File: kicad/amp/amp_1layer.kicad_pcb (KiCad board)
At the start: 2 copper layers, 145 x 120.3 mm, 126 parts, among them J1 DC 12V IN, J2 IN L-G-R, J3 SPK L, J4 SPK R, Q1001 BC547, Q1002 BC547, Q1003 BC557, Q1004 BD139, Q1005 BD140, Q1006 BC547, Q2001 BC547, Q2002 BC547, Q2003 BC557, Q2004 BD139, Q2005 BD140, Q2006 BC547

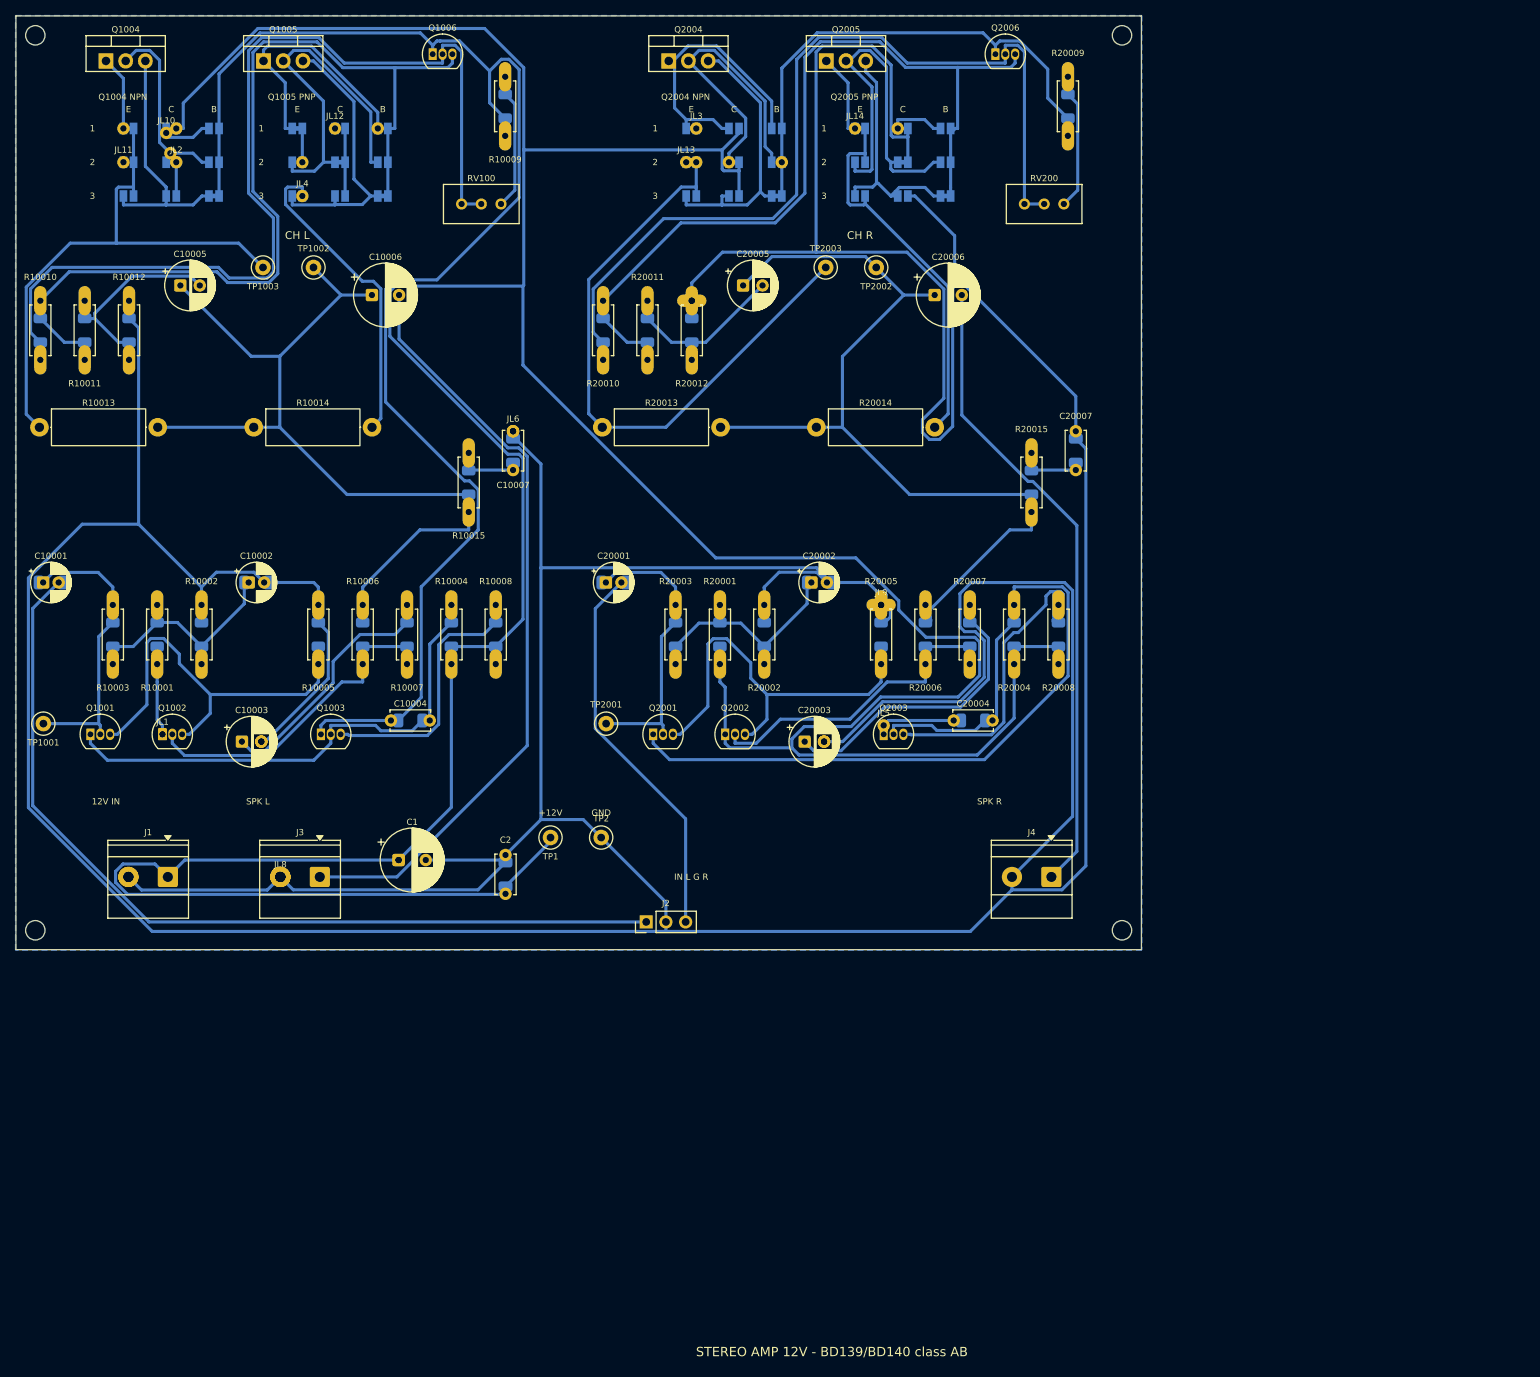
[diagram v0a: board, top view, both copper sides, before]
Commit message: Rotate screw terminals to face the board edge, add 3D views, schematics and layouts to the README, CircuitJS links in the review
Amp board is 100 x 85 mm after the hybrid-footprint courtyards grew; input header moved to open space
on the bottom edge so freerouting completes. Panel 134 x 137 mm, DRC clean.
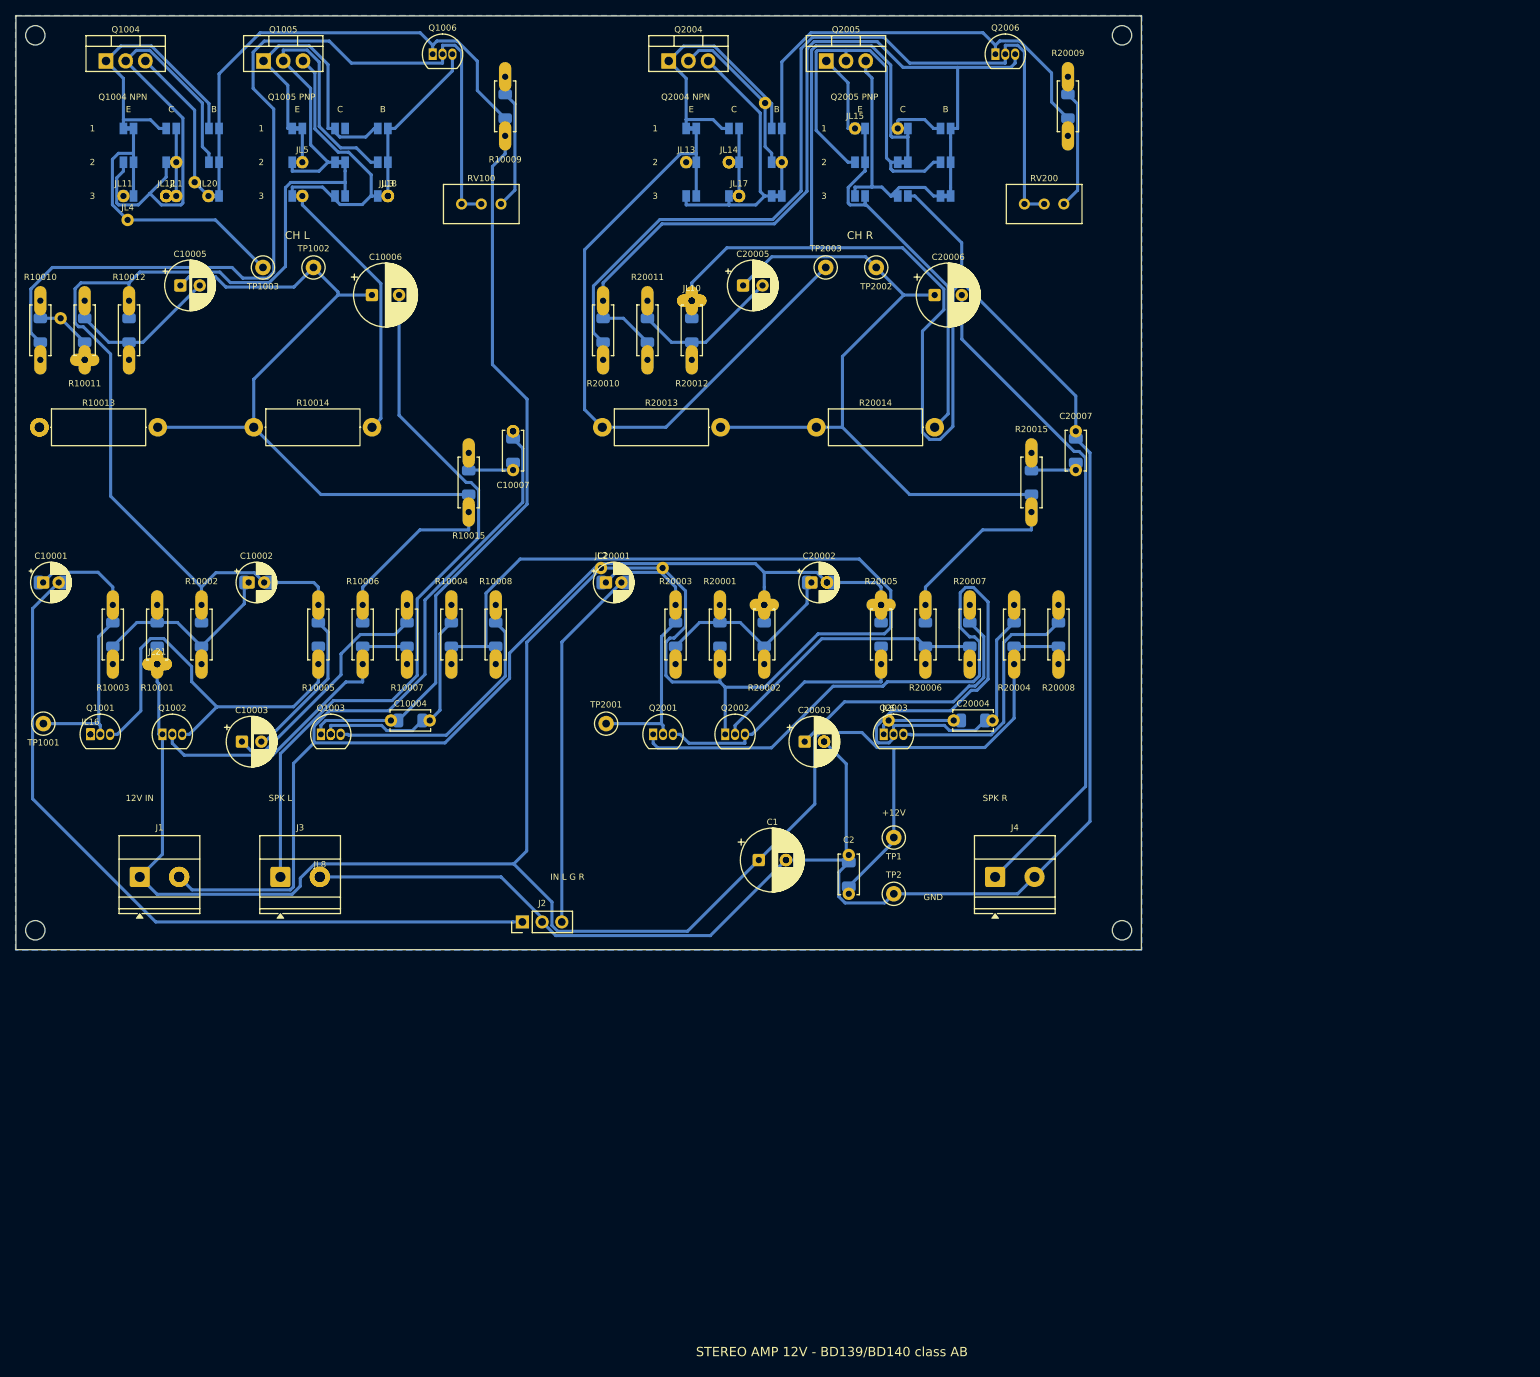
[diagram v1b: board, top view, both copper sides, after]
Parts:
- added JL15: wire link, Custom:WireLink, F.Cu at (158.1, 64.5)
- added JL16: wire link, Custom:WireLink, F.Cu at (59.6, 142.6)
- added JL17: wire link, Custom:WireLink, F.Cu at (143.2, 73.2)
- added JL18: wire link, Custom:WireLink, F.Cu at (97.9, 73.2)
- added JL19: wire link, Custom:WireLink, F.Cu at (149.2, 158.8)
- added JL20: wire link, Custom:WireLink, F.Cu at (74.8, 73.2)
- added JL21: wire link, Custom:WireLink, F.Cu at (68.2, 133.5)
- moved JL5 104.3 mm to (86.9, 68.8)
- moved JL2 75.7 mm to (125.4, 121.1)
- moved JL7 72.5 mm to (154.1, 143.5)
- moved JL10 71.1 mm to (137.1, 86.7)
- moved JL1 69.4 mm to (70.7, 73.2)
- moved JL6 61.1 mm to (162.4, 140.8)
- moved C1 46.4 mm to (145.7, 158.8)
- moved C2 44.2 mm to (157.3, 163.1)
- moved TP1 44.2 mm to (163.1, 155.8)
- moved JL3 40.7 mm to (97.9, 73.2)
- moved TP2 38.4 mm to (163.1, 163.1)
- moved JL12 23.4 mm to (69.4, 73.2)
- moved JL4 22.7 mm to (64.4, 76.3)
- moved JL14 16.8 mm to (141.9, 68.8)
- moved J2 15.9 mm to (115.2, 166.7)
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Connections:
- JL10 pad 1: Net-(JP10001-A) -> GND
- JL10 pad 2: Net-(JP10001-A) -> GND
- JL11 pad 1: Net-(JP10004-A) -> Net-(JP10007-A)
- JL11 pad 2: Net-(JP10004-A) -> Net-(JP10007-A)
- JL12 pad 1: Net-(JP10014-A) -> Net-(JP10007-A)
- JL12 pad 2: Net-(JP10014-A) -> Net-(JP10007-A)
- JL14 pad 1: Net-(JP20014-A) -> Net-(JP20004-A)
- JL14 pad 2: Net-(JP20014-A) -> Net-(JP20004-A)
- JL3 pad 1: /E4_R -> /B5_L
- JL3 pad 2: /E4_R -> /B5_L
- JL4 pad 1: /E5_L -> /E4_L
- JL4 pad 2: /E5_L -> /E4_L
- JL5 pad 1: /VAS_R -> /E5_L
- JL5 pad 2: /VAS_R -> /E5_L
- JL6 pad 1: GND -> /VAS_R
- JL6 pad 2: GND -> /VAS_R
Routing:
- net GND: track 828.3 -> 698.4 mm
- net +12V: track 535.2 -> 414.6 mm
- net /B5_L: track 121.0 -> 33.8 mm
- net Net-(JP10004-A): track 24.8 -> 63.0 mm
- net Net-(Q1001-C): track 65.9 -> 30.8 mm
- net /E4_L: track 70.9 -> 40.3 mm
- net /VAS_L: track 185.7 -> 161.5 mm
- net Net-(JP10001-A): track 16.8 -> 36.0 mm
- net Net-(JP20004-A): track 38.4 -> 21.2 mm
- net Net-(Q2001-E): track 52.9 -> 35.8 mm
- net /IN_L: track 115.9 -> 99.5 mm
- net Net-(Q2001-C): track 111.0 -> 126.5 mm
- net Net-(JP10007-A): track 32.3 -> 20.8 mm
- net /E4_R: track 80.2 -> 89.3 mm
- net Net-(Q2003-E): track 43.2 -> 34.3 mm
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
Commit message: Square 144 x 144 mm panel with rails; amp widened to 134 x 71 mm so PSU plus volume board match its width; readable silkscreen
References sit inside resistor, diode and ceramic outlines along the body axis, larger text; electrolytic,
transistor and test-point labels stay beside the part. Hybrid footprints built from the library parts keep
polarity marks. All 2-layer boards, the panel and the single-sided PSU and volume boards are DRC clean.
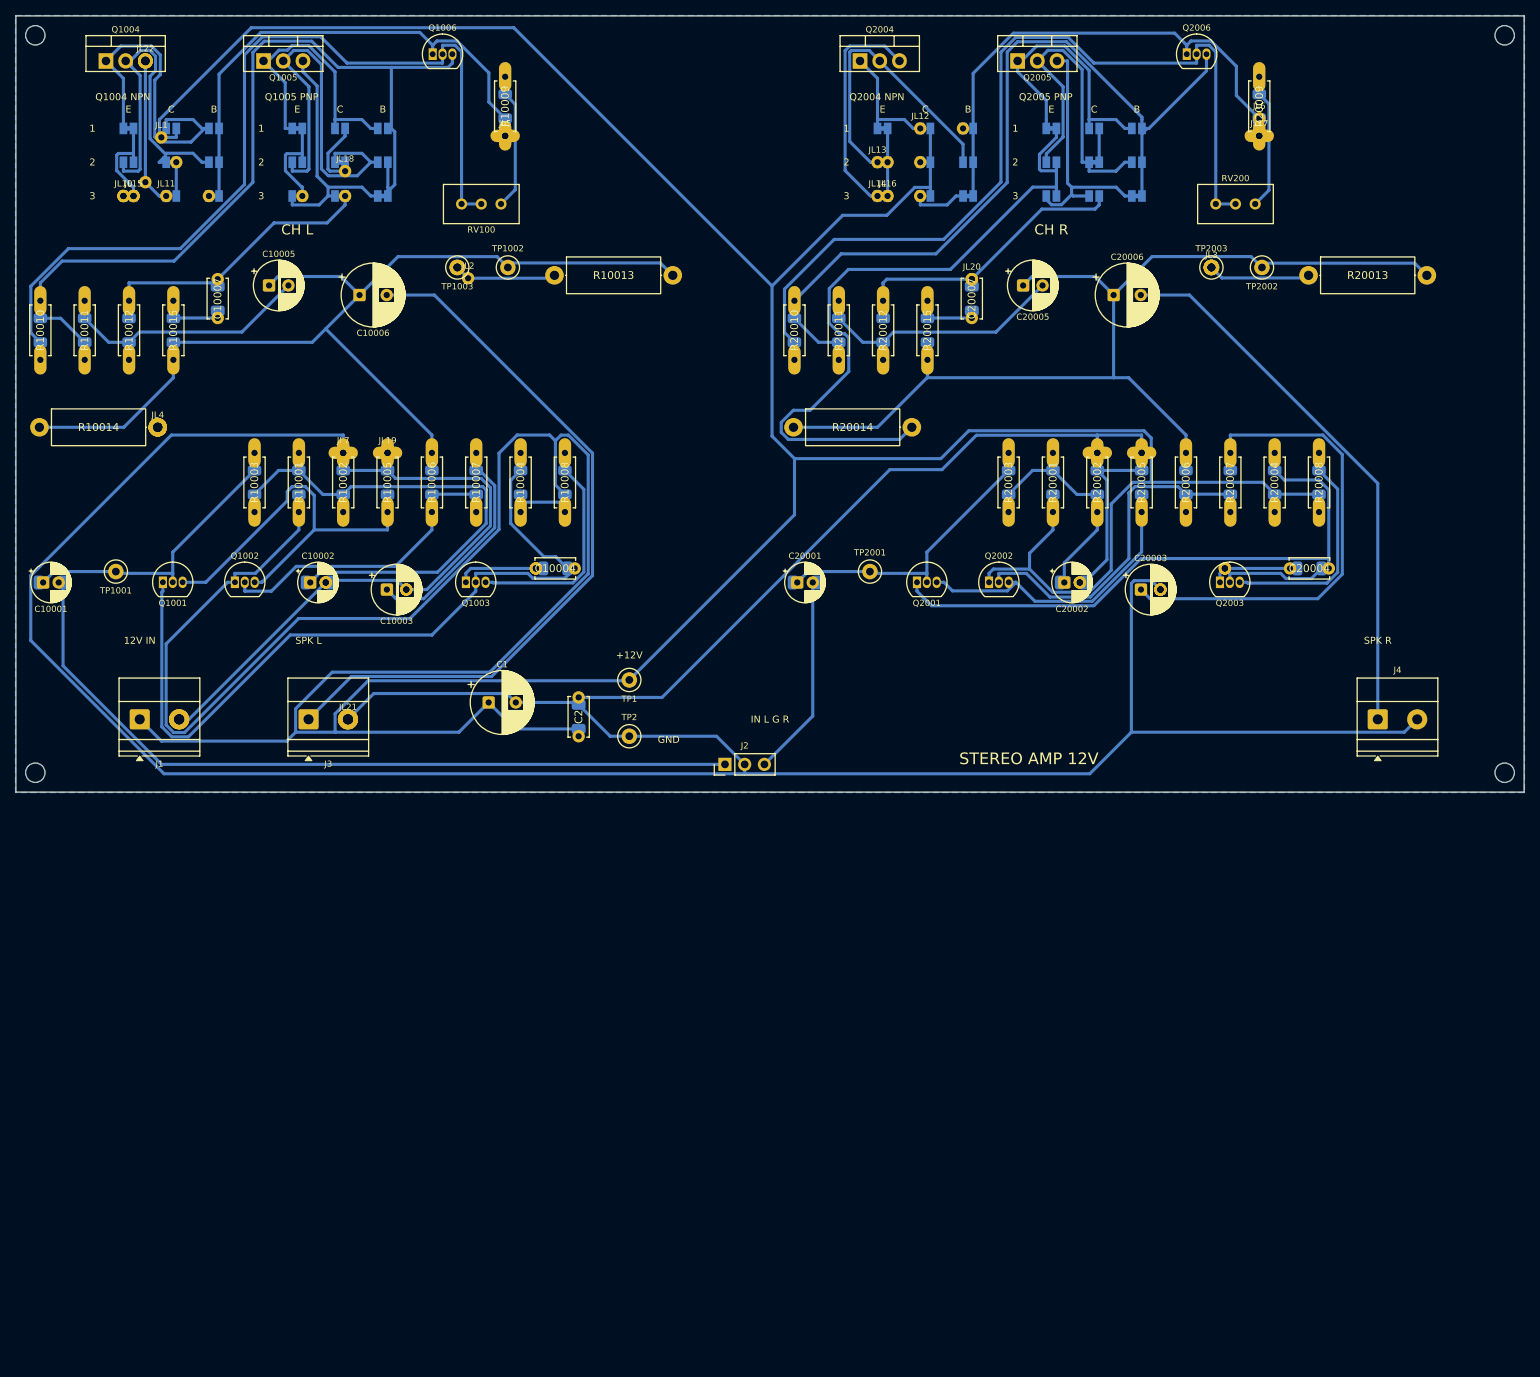
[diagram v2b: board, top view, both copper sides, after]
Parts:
- added JL22: wire link, Custom:WireLink, F.Cu at (66.7, 55.8)
- moved JL16 123.9 mm to (162.3, 73.2)
- moved JL8 114.4 mm to (197.4, 123.9)
- moved JL3 106.5 mm to (204.0, 82.4)
- moved JL20 98.9 mm to (173.1, 83.9)
- moved JL12 97.5 mm to (166.5, 64.5)
- moved JL15 93.4 mm to (65.2, 73.2)
- moved R20013 93.1 mm to (216.5, 83.4)
- moved JL6 91.1 mm to (210.2, 63.2)
- moved JL10 74.5 mm to (63.9, 73.2)
- moved JL19 73.4 mm to (97.9, 106.3)
- moved JL7 72.3 mm to (92.2, 106.3)
- moved R10013 69.2 mm to (119.4, 83.4)
- moved JL17 67.5 mm to (210.2, 65.5)
- moved H4 53.3 mm to (241.8, 147.5)
- moved J4 53.3 mm to (225.4, 140.6)
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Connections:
- JL10 pad 1: GND -> Net-(JP10007-A)
- JL10 pad 2: GND -> Net-(JP10007-A)
- JL12 pad 1: Net-(JP10007-A) -> Net-(JP20001-A)
- JL12 pad 2: Net-(JP10007-A) -> Net-(JP20001-A)
- JL14 pad 1: Net-(JP20004-A) -> Net-(JP20007-A)
- JL14 pad 2: Net-(JP20004-A) -> Net-(JP20007-A)
- JL15 pad 1: Net-(JP20014-A) -> /E4_L
- JL15 pad 2: Net-(JP20014-A) -> /E4_L
- JL16 pad 1: Net-(Q1001-C) -> /E4_R
- JL16 pad 2: Net-(Q1001-C) -> /E4_R
- JL17 pad 1: +12V -> /VAS_R
- JL17 pad 2: +12V -> /VAS_R
- JL18 pad 1: /B5_L -> GND
- JL18 pad 2: /B5_L -> GND
- JL2 pad 1: +12V -> /E4_L
- JL2 pad 2: +12V -> /E4_L
- JL20 pad 1: Net-(JP10007-A) -> GND
- JL20 pad 2: Net-(JP10007-A) -> GND
- JL21 pad 1: +12V -> GND
- JL21 pad 2: +12V -> GND
- JL3 pad 1: /B5_L -> /E4_R
- JL3 pad 2: /B5_L -> /E4_R
- JL4 pad 1: /E4_L -> /E5_L
- JL4 pad 2: /E4_L -> /E5_L
- JL5 pad 1: /E5_L -> /VAS_L
- JL5 pad 2: /E5_L -> /VAS_L
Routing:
- net +12V: track 414.6 -> 630.2 mm
- net /VAS_L: track 161.5 -> 76.8 mm
- net GND: track 698.4 -> 616.7 mm
- net /B5_L: track 33.8 -> 113.7 mm
- net Net-(Q1001-C): track 30.8 -> 103.5 mm
- net /E4_R: track 89.3 -> 21.9 mm
- net /E5_R: track 47.9 -> 90.1 mm
- net Net-(C10002-Pad1): track 31.9 -> 70.5 mm
- net Net-(Q2001-C): track 126.5 -> 92.6 mm
- net Net-(C20003-Pad1): track 36.6 -> 63.2 mm
- net /E5_L: track 38.8 -> 12.8 mm
- net /IN_R: track 47.5 -> 26.6 mm
- net Net-(JP20001-A): track 36.0 -> 15.6 mm
- net Net-(JP10004-A): track 63.0 -> 44.8 mm
- net Net-(JP20014-A): track 17.8 -> 35.2 mm
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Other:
- board size 145 x 120.3 mm -> 194.3 x 100 mm
- board text added: "STEREO AMP 12V"
- board text removed: "STEREO AMP 12V - BD139/BD140 class AB"

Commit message: Repository URL and revision on every silkscreen and on the panel rails
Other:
- board text added: "STEREO AMP 12V v1.0 2026-10"
- board text added: "github.com/lahirunirmalx/discrete-stereo-amp"
- board text removed: "STEREO AMP 12V"
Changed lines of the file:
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@@
+		)
+	)
+	(gr_text "github.com/lahirunirmalx/discrete-stereo-amp"
+		(at 188.95 143.65 0)
+		(layer "F.SilkS")
+		(effects
+			(font
+				(size 1 1)
+				(thickness 0.15)
+			)
 		)
 	)
@@
 		)
 	)
-	(gr_text "STEREO AMP 12V"
+	(gr_text "STEREO AMP 12V  v1.0 2026-10"
 		(at 180.5 145.7 0)
 		(layer "F.SilkS")

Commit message: Release 1.1: square panel, rotated terminals, readable silkscreen, URL and revision stamps
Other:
- board text added: "STEREO AMP 12V v1.1 2026-10"
- board text removed: "STEREO AMP 12V v1.0 2026-10"
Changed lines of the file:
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@@
 		)
 	)
-	(gr_text "STEREO AMP 12V  v1.0 2026-10"
+	(gr_text "STEREO AMP 12V  v1.1 2026-10"
 		(at 180.5 145.7 0)
 		(layer "F.SilkS")
